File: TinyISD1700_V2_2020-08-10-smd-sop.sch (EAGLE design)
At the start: 17 parts, among them IC1 REG1117, U1 ATTINY4313-SU

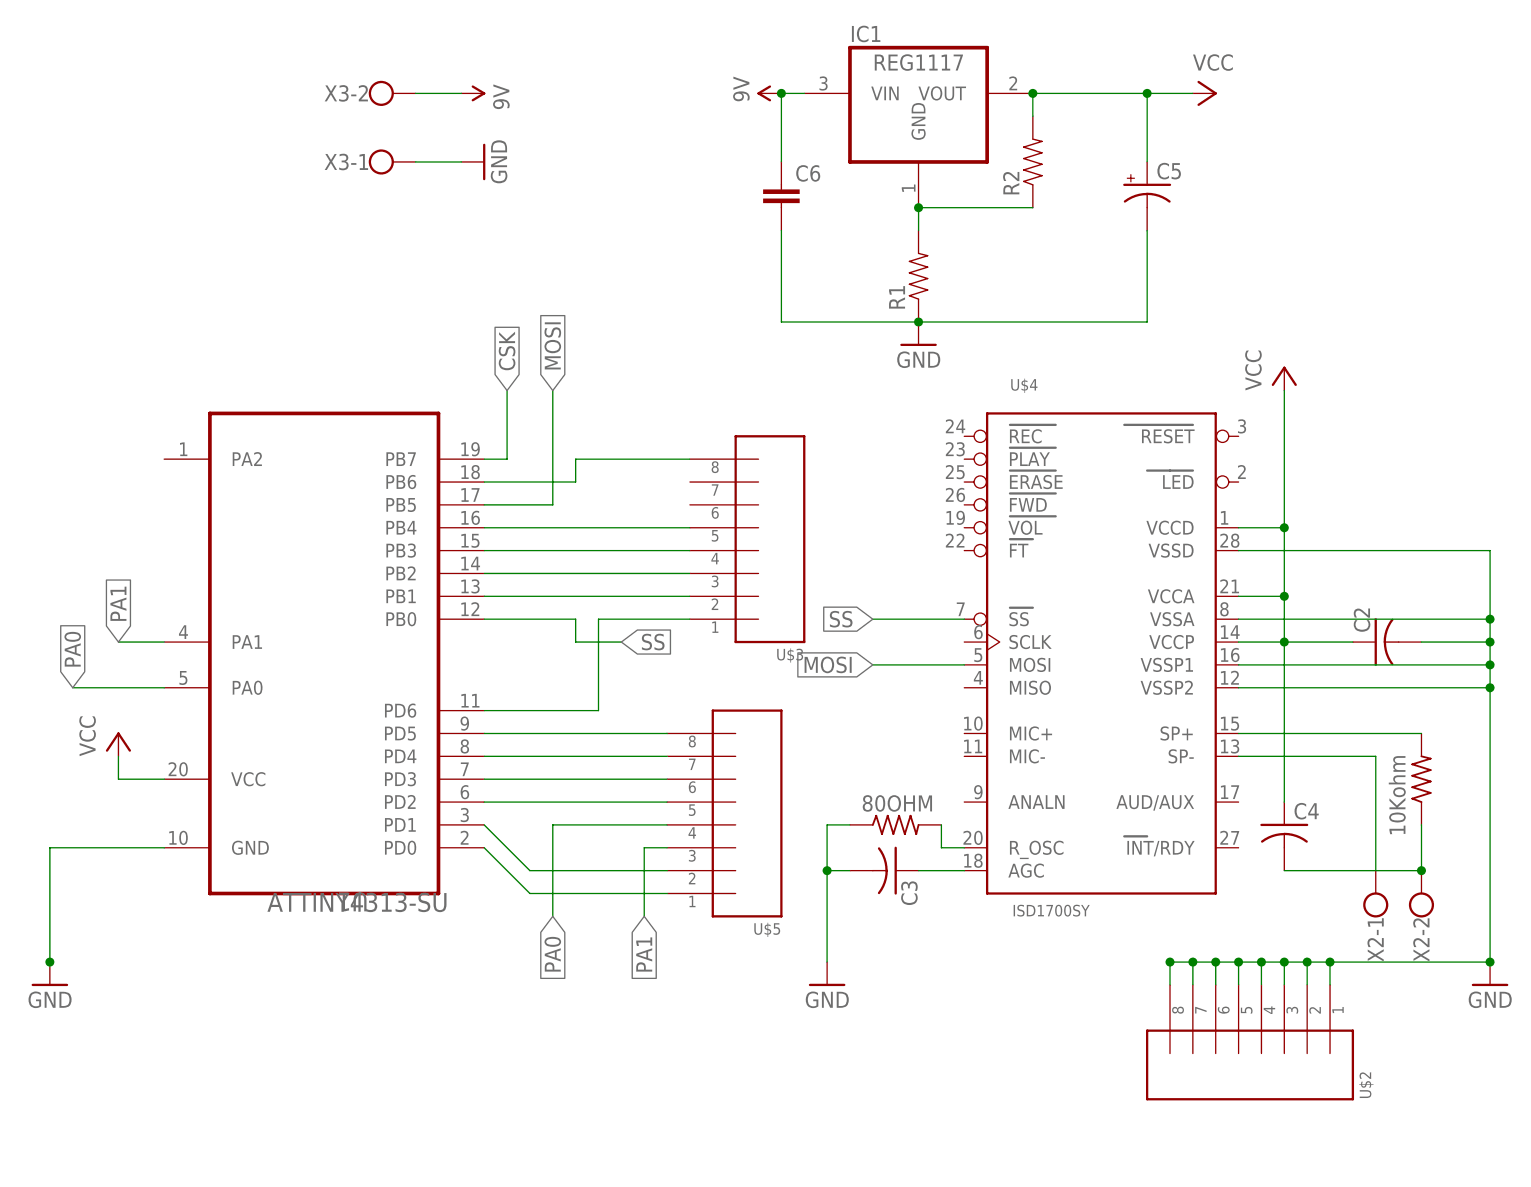
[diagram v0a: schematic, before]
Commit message: modefied regulator input
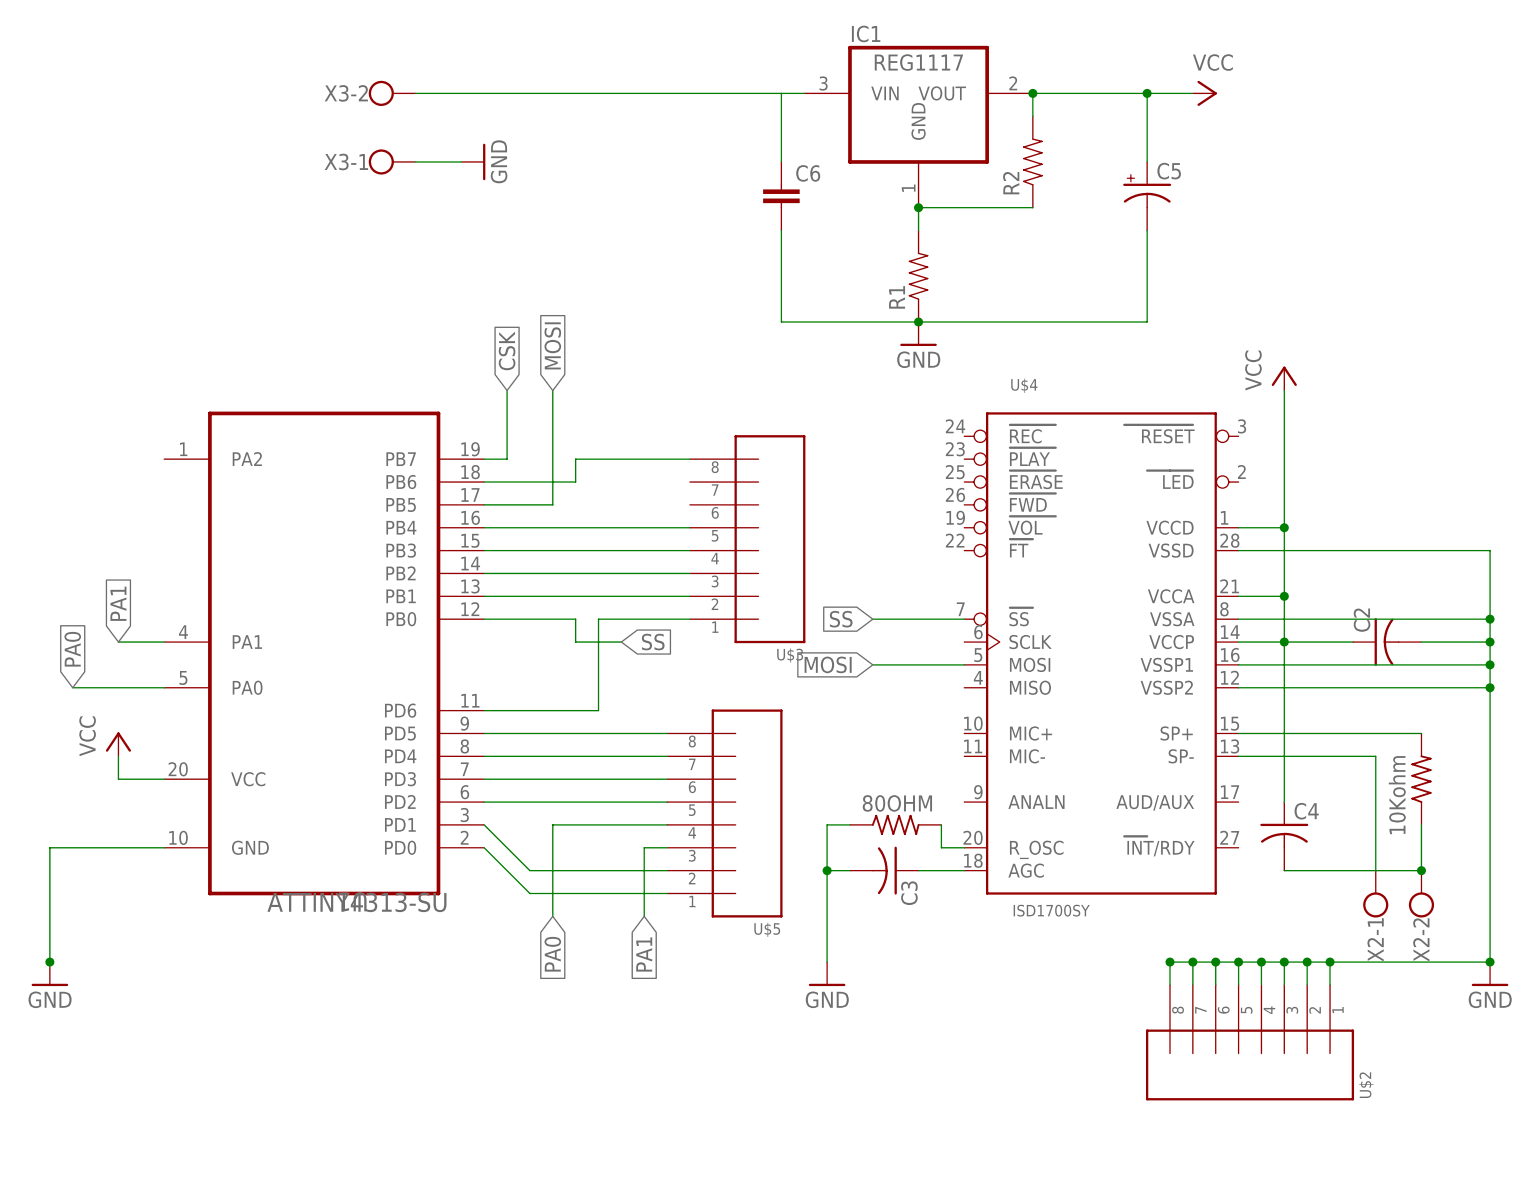
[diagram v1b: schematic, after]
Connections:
- net 5V renamed N$28

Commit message: bytt till MDT
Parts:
- removed IC1: REG1117, burr-brown:REG1117
- added IC3: LM317MDT, v-reg:LM317MDT
- added U$1: 8PIN_HEADER, arduino:8PIN_HEADER
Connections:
- net GND: now also U$1.P$1, U$1.P$2, U$1.P$3, U$1.P$4, U$1.P$5, U$1.P$6, U$1.P$7, U$1.P$8
- net N$28: no longer IC1.VIN
- net N$29: now also IC3.ADJ; no longer IC1.GND
- net VCC: now also IC3.OUT; no longer IC1.VOUT
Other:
- moved on the sheet: U$2
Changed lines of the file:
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@@
 <?xml version="1.0" encoding="utf-8"?>
 <!DOCTYPE eagle SYSTEM "eagle.dtd">
-<eagle version="9.4.2">
+<eagle version="6.4">
 <drawing>
 <settings>
 <setting alwaysvectorfont="no"/>
-<setting keepoldvectorfont="yes"/>
 <setting verticaltext="up"/>
 </settings>
@@
 <attribute name="MF" value="MICROCHIP"/>
 </part>
-<part name="IC1" library="burr-brown" deviceset="REG1117" device=""/>
 <part name="C6" library="SparkFun2" deviceset="CAP" device="0805"/>
 <part name="R1" library="SparkFun2" deviceset="RESISTOR" device=""/>
@@
 <part name="C5" library="SparkFun2" deviceset="CAP_POL" device="1206"/>
 <part name="GND5" library="supply1" deviceset="GND" device=""/>
+<part name="IC3" library="v-reg" deviceset="LM317?*" device="" technology="MDT"/>
+<part name="U$1" library="arduino" deviceset="8PIN_HEADER" device="">
+<attribute name="MF" value="RENESAS"/>
+<attribute name="MPN" value="YSDKS128E10"/>
+<attribute name="OC_FARNELL" value="2946736"/>
+</part>
 </parts>
 <sheets>
@@
 <attribute name="VALUE" x="10.16" y="45.72" size="1.778" layer="96" rot="R90"/>
 </instance>
-<instance part="U$2" gate="G$1" x="137.16" y="12.7" smashed="yes" rot="MR90">
-<attribute name="OC_FARNELL" x="137.16" y="12.7" size="1.778" layer="96" display="off"/>
-<attribute name="MF" x="137.16" y="12.7" size="1.778" layer="96" display="off"/>
-<attribute name="MPN" x="137.16" y="12.7" size="1.778" layer="96" display="off"/>
-<attribute name="NAME" x="150.622" y="7.62" size="1.27" layer="95" rot="MR90"/>
+<instance part="U$2" gate="G$1" x="137.16" y="5.08" smashed="yes" rot="MR90">
+<attribute name="OC_FARNELL" x="137.16" y="5.08" size="1.778" layer="96" display="off"/>
+<attribute name="MF" x="137.16" y="5.08" size="1.778" layer="96" display="off"/>
+<attribute name="MPN" x="137.16" y="5.08" size="1.778" layer="96" display="off"/>
+<attribute name="NAME" x="150.622" y="0" size="1.27" layer="95" rot="MR90"/>
 </instance>
 <instance part="GND4" gate="1" x="91.44" y="20.32" smashed="yes" rot="MR0">
@@
 <attribute name="VALUE" x="29.2354" y="28.448" size="2.0828" layer="96" ratio="10" rot="SR0"/>
 </instance>
-<instance part="IC1" gate="G$1" x="101.6" y="119.38" smashed="yes">
-<attribute name="NAME" x="93.98" y="125.095" size="1.778" layer="95" ratio="10"/>
-<attribute name="VALUE" x="96.52" y="121.92" size="1.778" layer="96" ratio="10"/>
-</instance>
 <instance part="C6" gate="G$1" x="86.36" y="106.68" smashed="yes">
 <attribute name="NAME" x="87.884" y="109.601" size="1.778" layer="95"/>
@@
 <instance part="GND5" gate="1" x="53.34" y="111.76" smashed="yes" rot="MR270">
 <attribute name="VALUE" x="55.88" y="114.3" size="1.778" layer="96" rot="MR270"/>
+</instance>
+<instance part="IC3" gate="G$1" x="101.6" y="119.38"/>
+<instance part="U$1" gate="G$1" x="139.7" y="22.86" smashed="yes" rot="MR270">
+<attribute name="OC_FARNELL" x="139.7" y="22.86" size="1.778" layer="96" rot="R180" display="off"/>
+<attribute name="MF" x="139.7" y="22.86" size="1.778" layer="96" rot="R180" display="off"/>
+<attribute name="MPN" x="139.7" y="22.86" size="1.778" layer="96" rot="R180" display="off"/>
+<attribute name="NAME" x="126.238" y="27.94" size="1.27" layer="95" rot="MR270"/>
 </instance>
 </instances>
@@
 </segment>
 <segment>
-<pinref part="IC1" gate="G$1" pin="VOUT"/>
 <pinref part="R2" gate="G$1" pin="2"/>
 <wire x1="114.3" y1="116.84" x2="114.3" y2="119.38" width="0.1524" layer="91"/>
 <wire x1="114.3" y1="119.38" x2="127" y2="119.38" width="0.1524" layer="91"/>
-<junction x="114.3" y="119.38"/>
 <wire x1="127" y1="119.38" x2="127" y2="111.76" width="0.1524" layer="91"/>
 <pinref part="C5" gate="G$1" pin="+"/>
@@
 <wire x1="127" y1="119.38" x2="132.08" y2="119.38" width="0.1524" layer="91"/>
 <junction x="127" y="119.38"/>
+<pinref part="IC3" gate="G$1" pin="OUT"/>
+<wire x1="109.22" y1="119.38" x2="114.3" y2="119.38" width="0.1524" layer="91"/>
+<junction x="114.3" y="119.38"/>
 </segment>
 </net>
@@
 <pinref part="GND2" gate="1" pin="GND"/>
 <pinref part="U$2" gate="G$1" pin="P$1"/>
-<wire x1="147.32" y1="20.32" x2="147.32" y2="22.86" width="0.1524" layer="91"/>
-<wire x1="147.32" y1="22.86" x2="165.1" y2="22.86" width="0.1524" layer="91"/>
+<wire x1="147.32" y1="12.7" x2="147.32" y2="15.24" width="0.1524" layer="91"/>
+<wire x1="147.32" y1="15.24" x2="165.1" y2="22.86" width="0.1524" layer="91"/>
 <pinref part="U$2" gate="G$1" pin="P$2"/>
-<wire x1="144.78" y1="20.32" x2="144.78" y2="22.86" width="0.1524" layer="91"/>
-<wire x1="147.32" y1="22.86" x2="144.78" y2="22.86" width="0.1524" layer="91"/>
+<wire x1="144.78" y1="12.7" x2="144.78" y2="15.24" width="0.1524" layer="91"/>
+<wire x1="147.32" y1="15.24" x2="144.78" y2="15.24" width="0.1524" layer="91"/>
 <pinref part="U$2" gate="G$1" pin="P$3"/>
-<wire x1="142.24" y1="20.32" x2="142.24" y2="22.86" width="0.1524" layer="91"/>
-<wire x1="144.78" y1="22.86" x2="142.24" y2="22.86" width="0.1524" layer="91"/>
+<wire x1="142.24" y1="12.7" x2="142.24" y2="15.24" width="0.1524" layer="91"/>
+<wire x1="144.78" y1="15.24" x2="142.24" y2="15.24" width="0.1524" layer="91"/>
 <pinref part="U$2" gate="G$1" pin="P$4"/>
-<wire x1="139.7" y1="20.32" x2="139.7" y2="22.86" width="0.1524" layer="91"/>
-<wire x1="142.24" y1="22.86" x2="139.7" y2="22.86" width="0.1524" layer="91"/>
+<wire x1="139.7" y1="12.7" x2="139.7" y2="15.24" width="0.1524" layer="91"/>
+<wire x1="142.24" y1="15.24" x2="139.7" y2="15.24" width="0.1524" layer="91"/>
 <pinref part="U$2" gate="G$1" pin="P$5"/>
-<wire x1="137.16" y1="20.32" x2="137.16" y2="22.86" width="0.1524" layer="91"/>
-<wire x1="139.7" y1="22.86" x2="137.16" y2="22.86" width="0.1524" layer="91"/>
+<wire x1="137.16" y1="12.7" x2="137.16" y2="15.24" width="0.1524" layer="91"/>
+<wire x1="139.7" y1="15.24" x2="137.16" y2="15.24" width="0.1524" layer="91"/>
 <pinref part="U$2" gate="G$1" pin="P$6"/>
-<wire x1="134.62" y1="20.32" x2="134.62" y2="22.86" width="0.1524" layer="91"/>
-<wire x1="137.16" y1="22.86" x2="134.62" y2="22.86" width="0.1524" layer="91"/>
+<wire x1="134.62" y1="12.7" x2="134.62" y2="15.24" width="0.1524" layer="91"/>
+<wire x1="137.16" y1="15.24" x2="134.62" y2="15.24" width="0.1524" layer="91"/>
 <pinref part="U$2" gate="G$1" pin="P$7"/>
-<wire x1="132.08" y1="20.32" x2="132.08" y2="22.86" width="0.1524" layer="91"/>
-<wire x1="134.62" y1="22.86" x2="132.08" y2="22.86" width="0.1524" layer="91"/>
+<wire x1="132.08" y1="12.7" x2="132.08" y2="15.24" width="0.1524" layer="91"/>
+<wire x1="134.62" y1="15.24" x2="132.08" y2="15.24" width="0.1524" layer="91"/>
 <pinref part="U$2" gate="G$1" pin="P$8"/>
-<wire x1="129.54" y1="20.32" x2="129.54" y2="22.86" width="0.1524" layer="91"/>
-<wire x1="132.08" y1="22.86" x2="129.54" y2="22.86" width="0.1524" layer="91"/>
-<junction x="129.54" y="22.86"/>
-<junction x="132.08" y="22.86"/>
-<junction x="134.62" y="22.86"/>
-<junction x="137.16" y="22.86"/>
-<junction x="139.7" y="22.86"/>
-<junction x="142.24" y="22.86"/>
-<junction x="144.78" y="22.86"/>
-<junction x="147.32" y="22.86"/>
+<wire x1="129.54" y1="12.7" x2="129.54" y2="15.24" width="0.1524" layer="91"/>
+<wire x1="132.08" y1="15.24" x2="129.54" y2="15.24" width="0.1524" layer="91"/>
+<junction x="129.54" y="15.24"/>
+<junction x="132.08" y="15.24"/>
+<junction x="134.62" y="15.24"/>
+<junction x="137.16" y="15.24"/>
+<junction x="139.7" y="15.24"/>
+<junction x="142.24" y="15.24"/>
+<junction x="144.78" y="15.24"/>
+<junction x="147.32" y="15.24"/>
 <pinref part="U$4" gate="G$1" pin="VSSD"/>
 <pinref part="U$4" gate="G$1" pin="VSSA"/>
 <pinref part="U$4" gate="G$1" pin="VSSP1"/>
 <pinref part="U$4" gate="G$1" pin="VSSP2"/>
+<pinref part="U$1" gate="G$1" pin="P$1"/>
+<pinref part="U$1" gate="G$1" pin="P$2"/>
+<pinref part="U$1" gate="G$1" pin="P$3"/>
+<pinref part="U$1" gate="G$1" pin="P$4"/>
+<pinref part="U$1" gate="G$1" pin="P$5"/>
+<pinref part="U$1" gate="G$1" pin="P$6"/>
+<pinref part="U$1" gate="G$1" pin="P$7"/>
+<pinref part="U$1" gate="G$1" pin="P$8"/>
 </segment>
 <segment>
@@
 <net name="N$29" class="0">
 <segment>
-<pinref part="IC1" gate="G$1" pin="GND"/>
 <pinref part="R1" gate="G$1" pin="2"/>
 <wire x1="101.6" y1="104.14" x2="101.6" y2="106.68" width="0.1524" layer="91"/>
 <pinref part="R2" gate="G$1" pin="1"/>
 <wire x1="101.6" y1="106.68" x2="114.3" y2="106.68" width="0.1524" layer="91"/>
+<pinref part="IC3" gate="G$1" pin="ADJ"/>
+<wire x1="101.6" y1="111.76" x2="101.6" y2="106.68" width="0.1524" layer="91"/>
 <junction x="101.6" y="106.68"/>
 </segment>
@@
 <pinref part="C6" gate="G$1" pin="1"/>
 <wire x1="86.36" y1="111.76" x2="86.36" y2="119.38" width="0.1524" layer="91"/>
-<pinref part="IC1" gate="G$1" pin="VIN"/>
-<wire x1="86.36" y1="119.38" x2="88.9" y2="119.38" width="0.1524" layer="91"/>
+<wire x1="86.36" y1="119.38" x2="93.98" y2="119.38" width="0.1524" layer="91"/>
 <pinref part="X3" gate="-2" pin="KL"/>
 <wire x1="86.36" y1="119.38" x2="45.72" y2="119.38" width="0.1524" layer="91"/>

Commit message: added values
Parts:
- C5: value (none) -> 1uF
- C6: value (none) -> 0.1uF
- R1: value (none) -> 240OHM
- R2: value (none) -> 340OHM
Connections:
- net GND: now also R2.1; no longer R1.1
- net N$28: now also IC3.IN
- net N$29: now also R1.1, R2.2; no longer R1.2, R2.1
- net VCC: now also R1.2; no longer R2.2
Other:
- moved on the sheet: R1, R2
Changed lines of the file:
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@@
 <?xml version="1.0" encoding="utf-8"?>
 <!DOCTYPE eagle SYSTEM "eagle.dtd">
-<eagle version="6.4">
+<eagle version="9.4.2">
 <drawing>
 <settings>
 <setting alwaysvectorfont="no"/>
+<setting keepoldvectorfont="yes"/>
 <setting verticaltext="up"/>
 </settings>
@@
 <attribute name="MF" value="MICROCHIP"/>
 </part>
-<part name="C6" library="SparkFun2" deviceset="CAP" device="0805"/>
-<part name="R1" library="SparkFun2" deviceset="RESISTOR" device=""/>
-<part name="R2" library="SparkFun2" deviceset="RESISTOR" device=""/>
+<part name="C6" library="SparkFun2" deviceset="CAP" device="0805" value="0.1uF"/>
+<part name="R2" library="SparkFun2" deviceset="RESISTOR" device="" value="340OHM"/>
+<part name="R1" library="SparkFun2" deviceset="RESISTOR" device="" value="240OHM"/>
 <part name="GND3" library="supply1" deviceset="GND" device=""/>
 <part name="P+3" library="supply1" deviceset="VCC" device=""/>
-<part name="C5" library="SparkFun2" deviceset="CAP_POL" device="1206"/>
+<part name="C5" library="SparkFun2" deviceset="CAP_POL" device="1206" value="1uF"/>
 <part name="GND5" library="supply1" deviceset="GND" device=""/>
 <part name="IC3" library="v-reg" deviceset="LM317?*" device="" technology="MDT"/>
@@
 <attribute name="VALUE" x="87.884" y="104.521" size="1.778" layer="96"/>
 </instance>
-<instance part="R1" gate="G$1" x="101.6" y="99.06" smashed="yes" rot="R90">
+<instance part="R2" gate="G$1" x="101.6" y="99.06" smashed="yes" rot="R90">
 <attribute name="NAME" x="100.1014" y="95.25" size="1.778" layer="95" rot="R90"/>
 <attribute name="VALUE" x="104.902" y="95.25" size="1.778" layer="96" rot="R90"/>
 </instance>
-<instance part="R2" gate="G$1" x="114.3" y="111.76" smashed="yes" rot="R90">
-<attribute name="NAME" x="112.8014" y="107.95" size="1.778" layer="95" rot="R90"/>
+<instance part="R1" gate="G$1" x="114.3" y="111.76" smashed="yes" rot="R90">
+<attribute name="NAME" x="112.8014" y="110.49" size="1.778" layer="95" rot="R90"/>
 <attribute name="VALUE" x="117.602" y="107.95" size="1.778" layer="96" rot="R90"/>
 </instance>
@@
 <attribute name="VALUE" x="55.88" y="114.3" size="1.778" layer="96" rot="MR270"/>
 </instance>
-<instance part="IC3" gate="G$1" x="101.6" y="119.38"/>
+<instance part="IC3" gate="G$1" x="101.6" y="119.38" smashed="yes">
+<attribute name="NAME" x="88.9" y="121.92" size="1.778" layer="95"/>
+<attribute name="VALUE" x="93.98" y="121.92" size="1.778" layer="96"/>
+</instance>
 <instance part="U$1" gate="G$1" x="139.7" y="22.86" smashed="yes" rot="MR270">
 <attribute name="OC_FARNELL" x="139.7" y="22.86" size="1.778" layer="96" rot="R180" display="off"/>
@@
 </segment>
 <segment>
-<pinref part="R2" gate="G$1" pin="2"/>
+<pinref part="R1" gate="G$1" pin="2"/>
 <wire x1="114.3" y1="116.84" x2="114.3" y2="119.38" width="0.1524" layer="91"/>
 <wire x1="114.3" y1="119.38" x2="127" y2="119.38" width="0.1524" layer="91"/>
@@
 <segment>
 <wire x1="127" y1="104.14" x2="127" y2="93.98" width="0.1524" layer="91"/>
-<pinref part="R1" gate="G$1" pin="1"/>
+<pinref part="R2" gate="G$1" pin="1"/>
 <wire x1="127" y1="93.98" x2="101.6" y2="93.98" width="0.1524" layer="91"/>
 <wire x1="101.6" y1="93.98" x2="86.36" y2="93.98" width="0.1524" layer="91"/>
@@
 <net name="N$29" class="0">
 <segment>
-<pinref part="R1" gate="G$1" pin="2"/>
+<pinref part="R2" gate="G$1" pin="2"/>
 <wire x1="101.6" y1="104.14" x2="101.6" y2="106.68" width="0.1524" layer="91"/>
-<pinref part="R2" gate="G$1" pin="1"/>
+<pinref part="R1" gate="G$1" pin="1"/>
 <wire x1="101.6" y1="106.68" x2="114.3" y2="106.68" width="0.1524" layer="91"/>
 <pinref part="IC3" gate="G$1" pin="ADJ"/>
@@
 <pinref part="X3" gate="-2" pin="KL"/>
 <wire x1="86.36" y1="119.38" x2="45.72" y2="119.38" width="0.1524" layer="91"/>
-</segment>
-</net>
+<pinref part="IC3" gate="G$1" pin="IN"/>
+</segment>
+</net>
